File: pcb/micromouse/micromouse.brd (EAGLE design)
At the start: 80 x 115 mm, 66 parts, among them IC1 LM2575-5.0WU-(TR), IC2 LM2575-3.3WU-(TR), IC3 DSPIC33FJ64MC804-PT, IC4 L293D, Y1 7.3728MHz

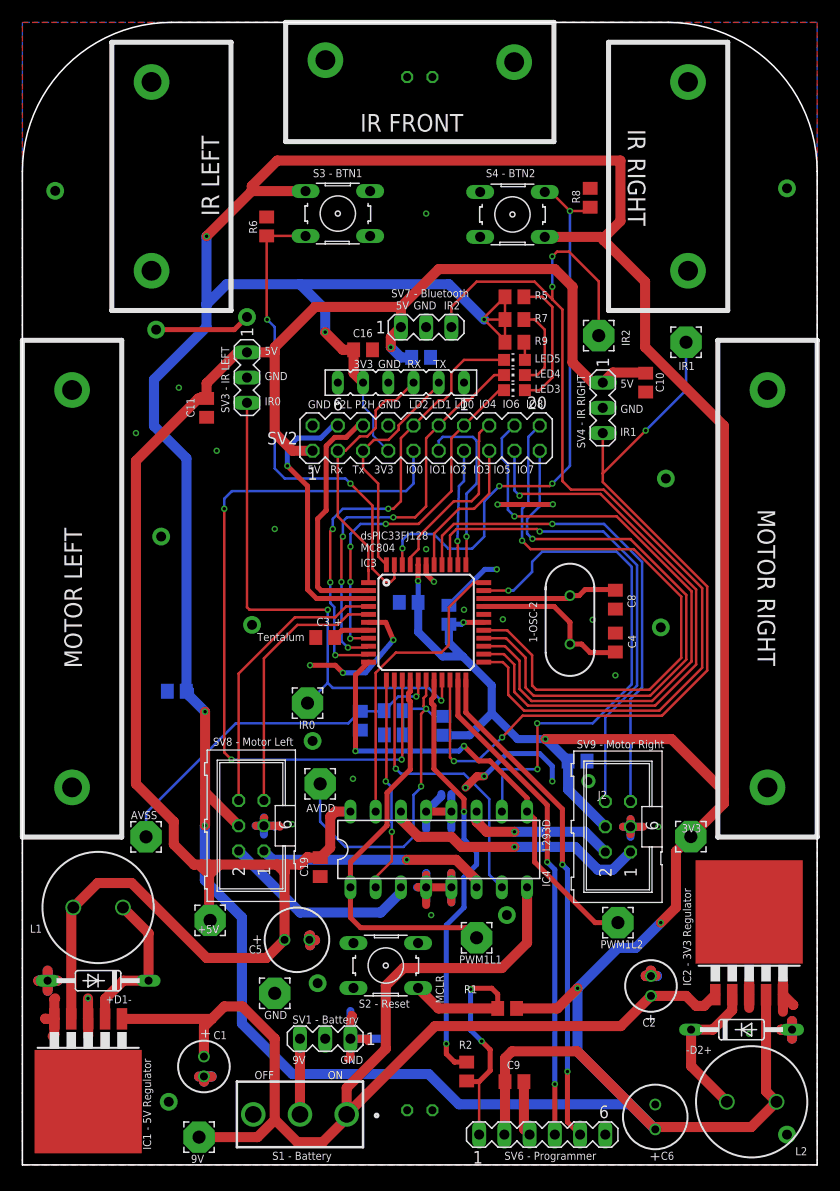
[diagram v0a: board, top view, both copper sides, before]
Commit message: Add 100nF capacitors at inputs and outputs of both switching converters. Add vias for ground stitching.
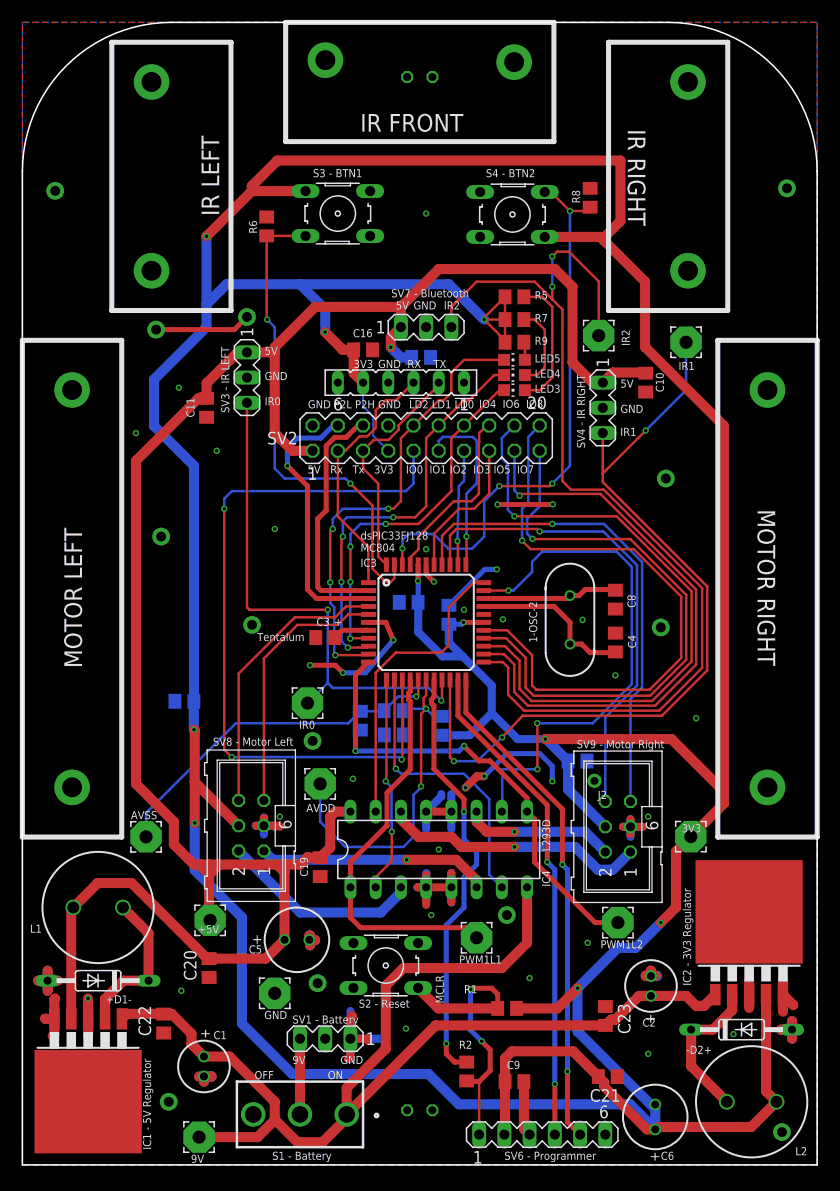
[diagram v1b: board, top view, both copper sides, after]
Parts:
- added C20, C21, C22, C23: 100nF, rcl:C0805
- moved C17 1.27 mm to (16.3, 46.7)
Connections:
- net +3V3: now also C21.2
- net +5V: now also C20.2
- net +9V: now also C22.2, C23.2
- net GND: now also C20.1, C21.1, C22.1, C23.1
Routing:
- net +9V: track 126.5 -> 118.7 mm
- net +3V3: track 499.0 -> 500.5 mm

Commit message: Fix minor issues from previous commit.
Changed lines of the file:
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@@
 <drawing>
 <settings>
-<setting alwaysvectorfont="yes"/>
+<setting alwaysvectorfont="no"/>
 <setting verticaltext="up"/>
 </settings>
@@
 <wire x1="70.612" y1="37.592" x2="70.612" y2="36.3728" width="1.016" layer="1"/>
 <wire x1="55.88" y1="17.78" x2="55.88" y2="13.4312" width="1.016" layer="16"/>
-<wire x1="63.7032" y1="5.608" x2="63.7032" y2="3.576" width="1.016" layer="16"/>
-<wire x1="63.7032" y1="5.608" x2="55.88" y2="13.4312" width="1.016" layer="16"/>
+<wire x1="62.4332" y1="6.878" x2="62.4332" y2="4.846" width="1.016" layer="16"/>
+<wire x1="62.4332" y1="4.846" x2="63.7032" y2="3.576" width="1.016" layer="16"/>
+<wire x1="62.4332" y1="6.878" x2="55.88" y2="13.4312" width="1.016" layer="16"/>
 <wire x1="63.7032" y1="3.576" x2="61.1832" y2="6.096" width="1.016" layer="16"/>
 <wire x1="61.1832" y1="6.096" x2="43.942" y2="6.096" width="1.016" layer="16"/>
@@
 <wire x1="25.44785625" y1="4.52414375" x2="27.686" y2="2.286" width="1.016" layer="1"/>
 <wire x1="27.686" y1="2.286" x2="30.226" y2="2.286" width="1.016" layer="1"/>
-<wire x1="10.5316" y1="15.2052" x2="10.0236" y2="14.6972" width="1.016" layer="1"/>
 <wire x1="30.226" y1="2.286" x2="32.64" y2="4.7" width="1.016" layer="1"/>
 <wire x1="32.64" y1="4.7" x2="32.64" y2="5.08" width="1.016" layer="1"/>
@@
 <wire x1="20.844" y1="10.906" x2="18.272" y2="10.906" width="1.016" layer="1"/>
 <wire x1="18.272" y1="10.906" x2="17.018" y2="12.16" width="1.016" layer="1"/>
-<wire x1="17.018" y1="12.16" x2="17.018" y2="13.208" width="1.016" layer="1"/>
-<wire x1="17.018" y1="13.208" x2="15.0208" y2="15.2052" width="1.016" layer="1"/>
-<wire x1="15.0208" y1="15.2052" x2="10.5316" y2="15.2052" width="1.016" layer="1"/>
+<wire x1="17.018" y1="13.208" x2="17.018" y2="12.16" width="1.016" layer="1"/>
 <wire x1="41.596" y1="14.036" x2="58.674" y2="14.036" width="1.016" layer="1"/>
 <wire x1="32.64" y1="5.08" x2="41.596" y2="14.036" width="1.016" layer="1"/>
@@
 <wire x1="62.07715" y1="17.0086" x2="63.2714" y2="17.0086" width="1.016" layer="1"/>
 <wire x1="59.69655" y1="14.628" x2="62.07715" y2="17.0086" width="1.016" layer="1"/>
-<wire x1="10.0236" y1="14.6972" x2="14.224" y2="15.174" width="0" layer="19" extent="1-1"/>
+<wire x1="14.224" y1="15.174" x2="15.052" y2="15.174" width="1.016" layer="1"/>
+<wire x1="15.052" y1="15.174" x2="17.018" y2="13.208" width="1.016" layer="1"/>
+<wire x1="10.0236" y1="14.6972" x2="10.5004" y2="15.174" width="1.016" layer="1"/>
+<wire x1="10.5004" y1="15.174" x2="14.224" y2="15.174" width="1.016" layer="1"/>
 </signal>
 <signal name="N$4">

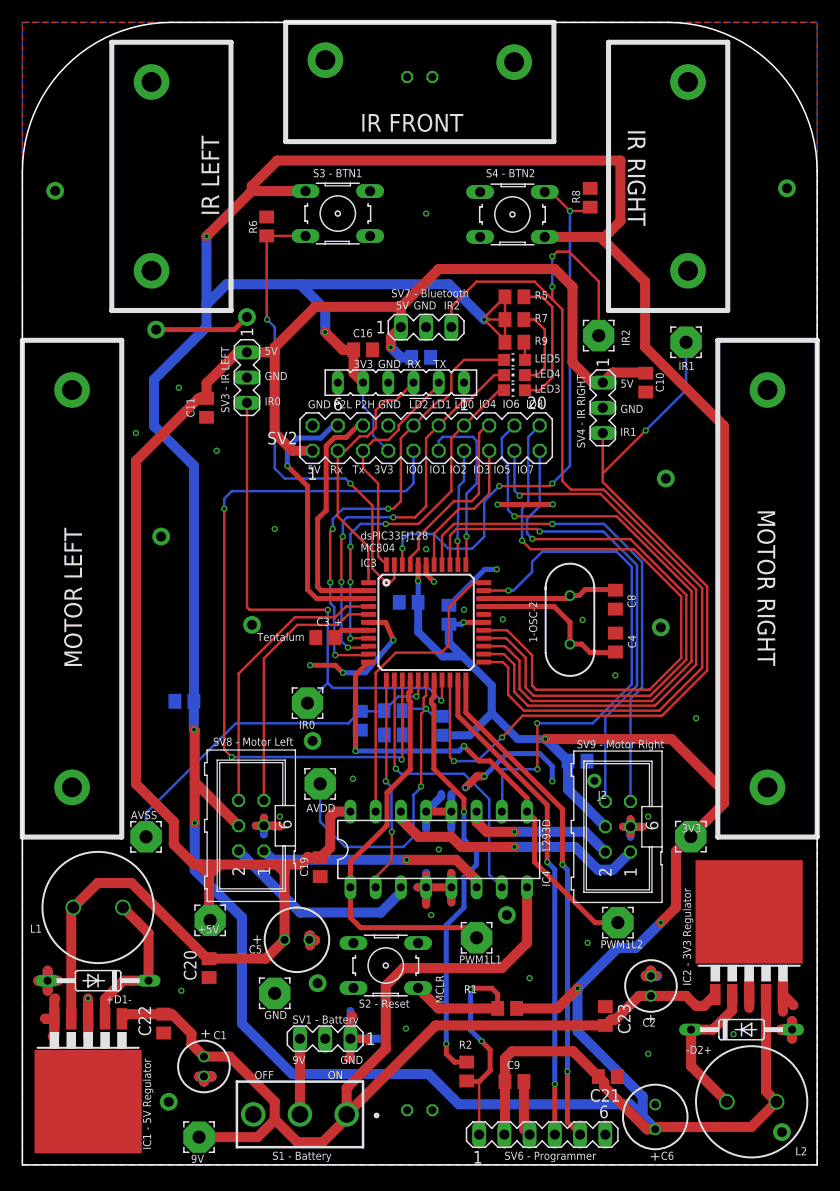
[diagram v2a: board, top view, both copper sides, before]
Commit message: Move 100nF capacitors of switching converters close to the input/output of the converters. Connect stitching vias to GND. Activate ground plane (ratsnest).
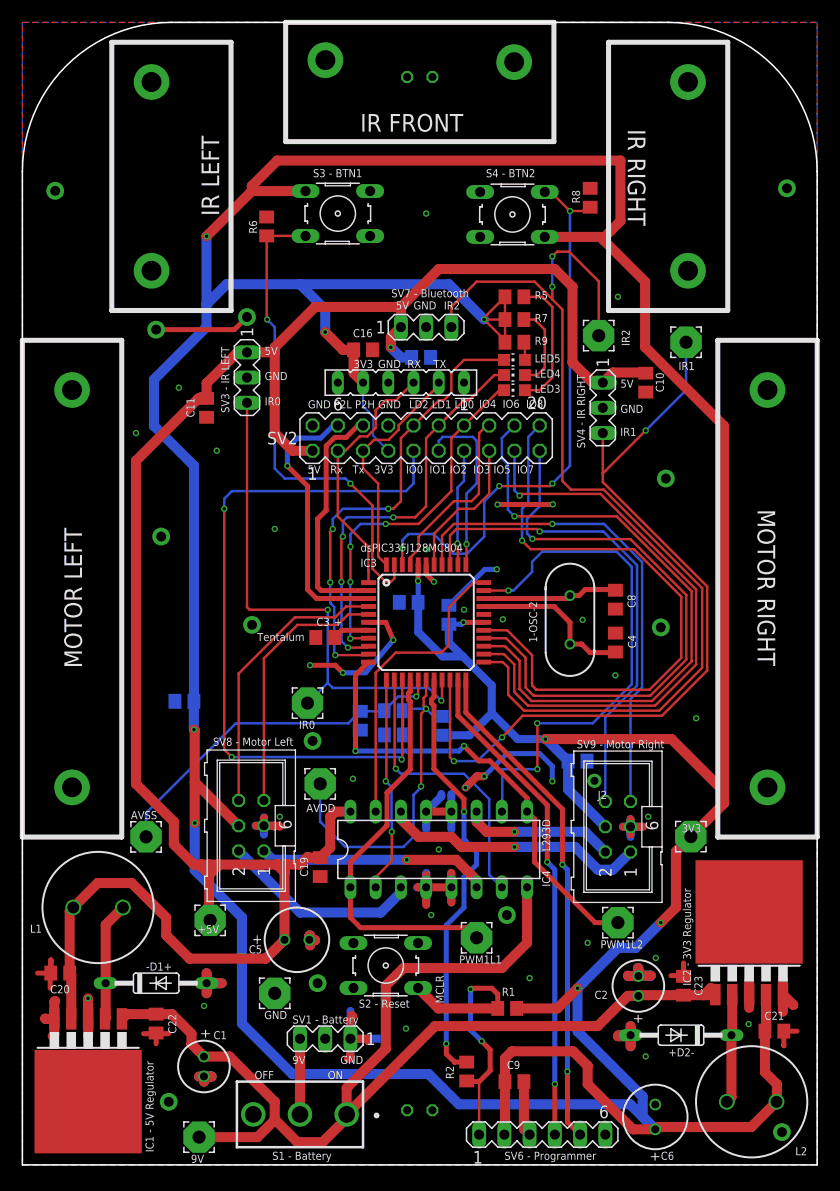
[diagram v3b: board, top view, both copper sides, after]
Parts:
- moved C21 17.4 mm to (75.7, 13.5)
- moved C20 15.0 mm to (3.81, 19.3), turned to 0 degrees
- moved C23 8.44 mm to (66.5, 18.0)
- moved D2 6.12 mm to (66.3, 13.1), turned to 180 degrees
- moved D1 5.85 mm to (13.5, 18.3), turned to 0 degrees
- moved C2 1.27 mm to (62.0, 18.0)
- moved C22 0.76 mm to (13.5, 14.2)
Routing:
- net GND: track 150.7 -> 171.5 mm, vias 49 -> 58
- net N$8: track 15.3 -> 11.0 mm
- net N$7: track 15.6 -> 12.0 mm
- net +5V: track 207.4 -> 208.9 mm
- net +3V3: track 500.5 -> 501.4 mm
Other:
- board text added: "+D2-"
- board text added: "-D1+"
- board text added: "C20"
- board text added: "C21"
- board text added: "C22"
- board text added: "C23"
- board text added: "dsPIC33FJ128MC804"
- board text removed: "+D1-"
- board text removed: "-D2+"
- board text removed: "dsPIC33FJ128 MC804"
